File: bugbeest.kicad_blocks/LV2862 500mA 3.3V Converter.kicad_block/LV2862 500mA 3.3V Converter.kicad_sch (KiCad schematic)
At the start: 14 parts, among them U1 LV2862YDDC

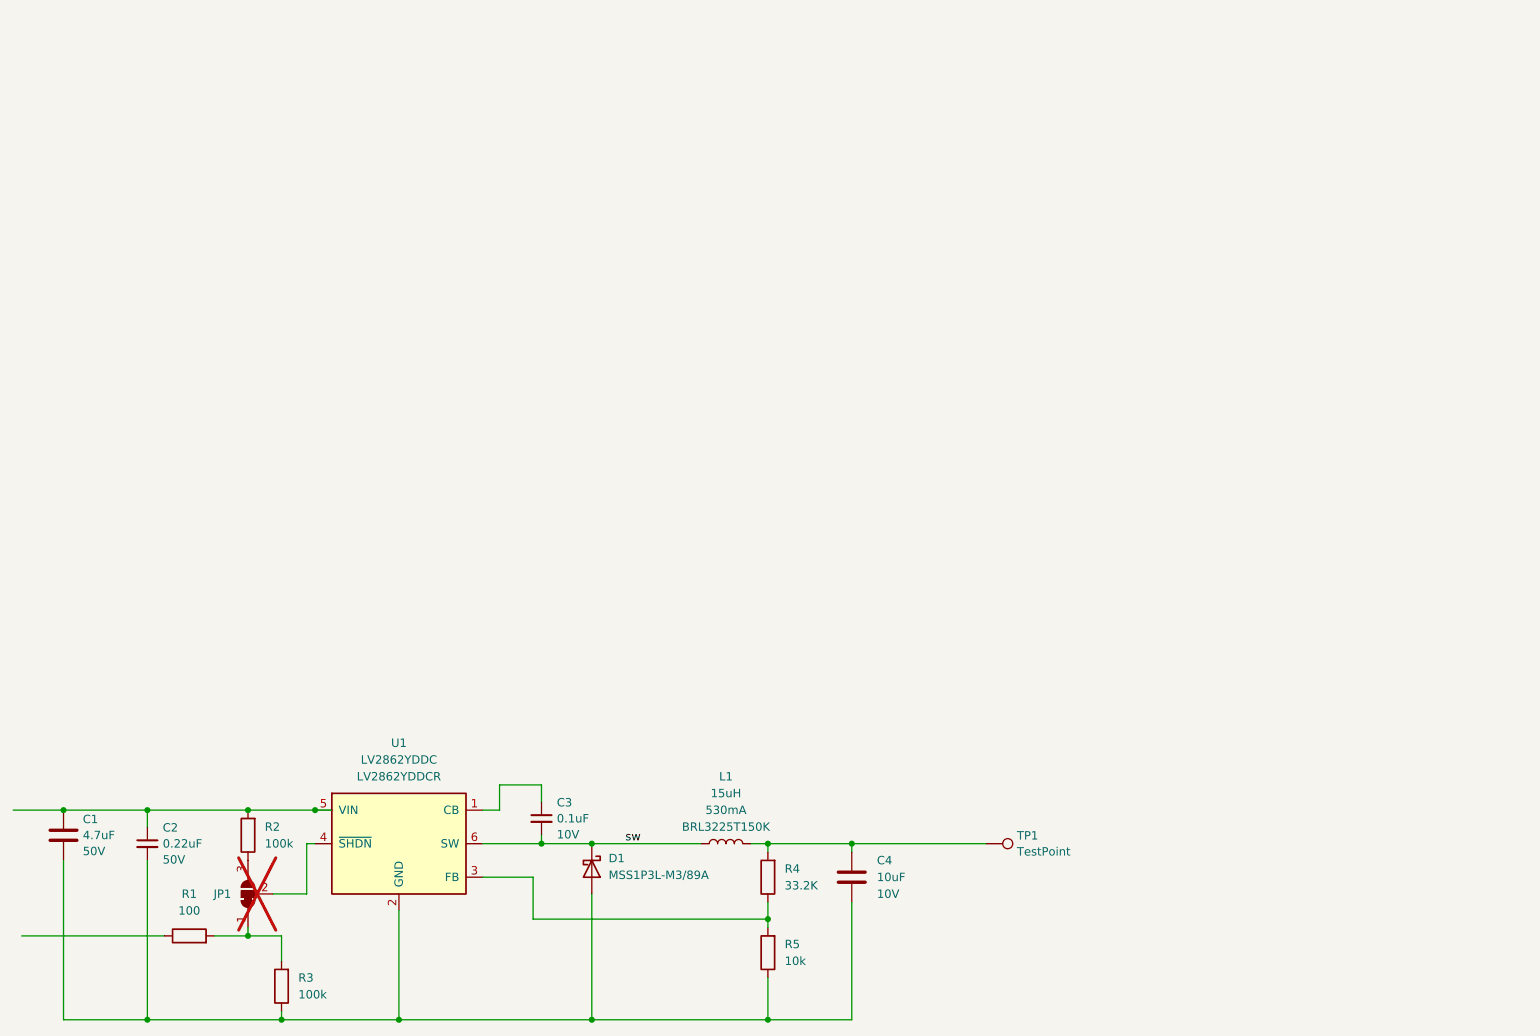
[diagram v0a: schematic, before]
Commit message: debugged design blocks, added encoder footprint
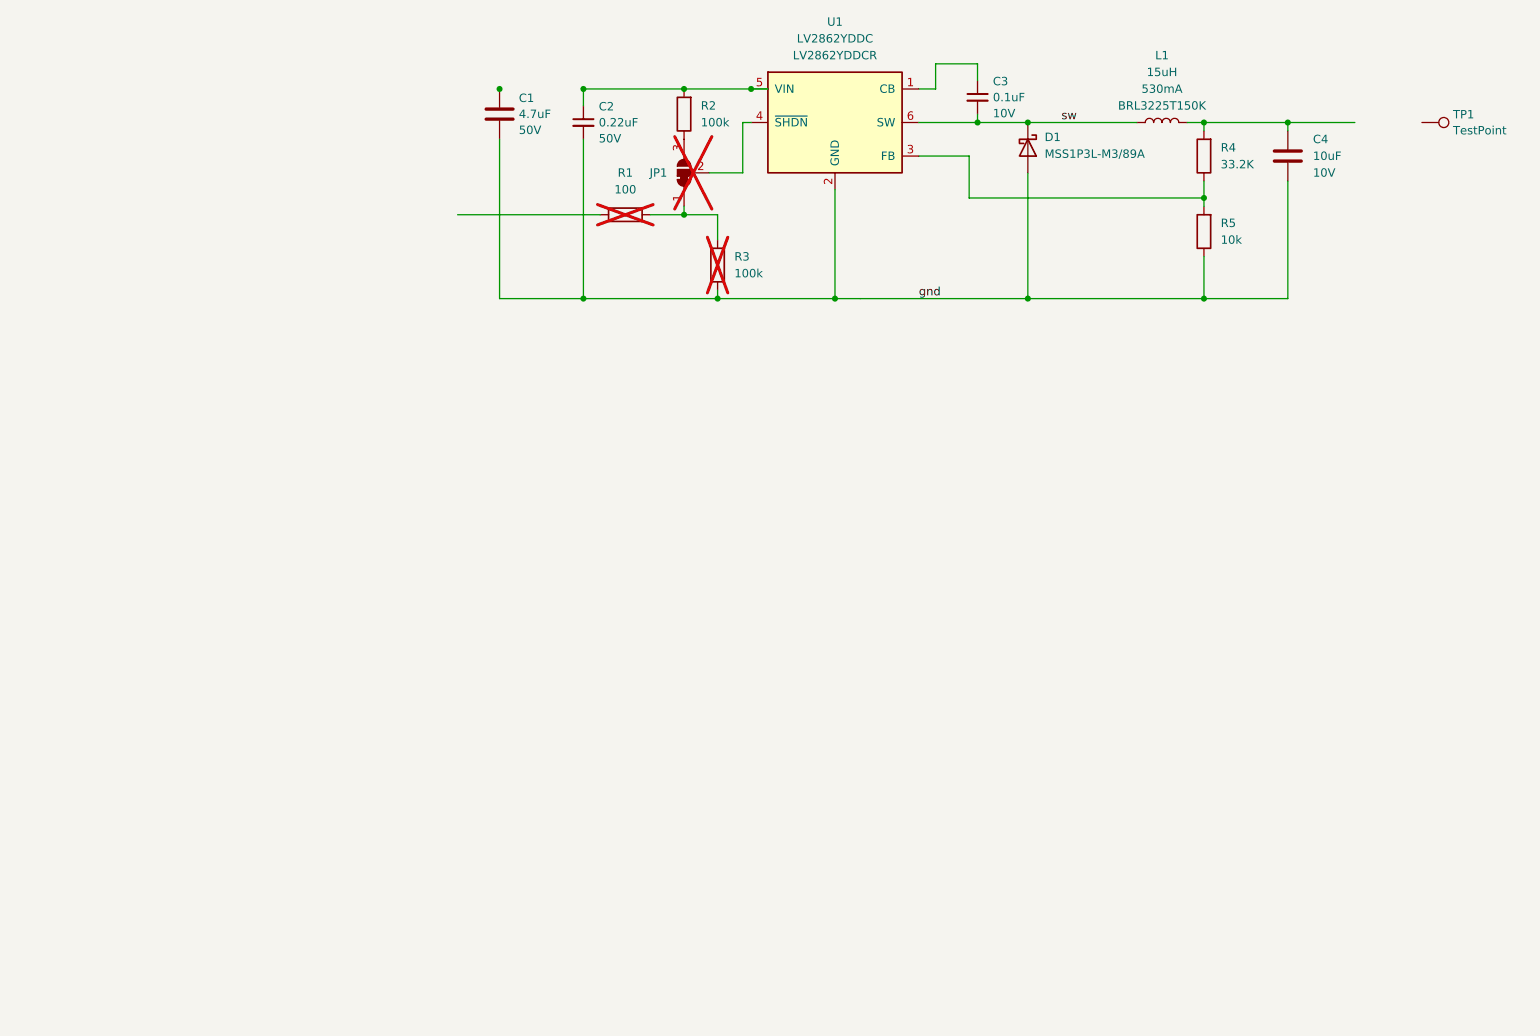
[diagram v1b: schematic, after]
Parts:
- R1, R3: now not fitted
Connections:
- net at C2.1, R2.2, U1.5 (VIN): no longer C1.1
- net gnd: now reaches C1.2, C2.2, C4.2, D1.2 (A), R3.1, R5.1, U1.2 (GND)
- net at C4.1, L1.2, R4.2: no longer TP1.1
